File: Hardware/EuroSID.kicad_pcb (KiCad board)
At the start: 2 copper layers, 212.3 x 100 mm, 228 parts, among them J1 GATE_2, J10 IN_2, J11 IN_3, J12 PWM_CV, J13 EXT_CON, J14 Conn_01x04_Female, J15 Eurorack Connector, J16 Conn_01x06_Male, J17 Conn_ARM_JTAG_SWD_10, J18 Power_Connector_IO, J19 Power_Connector, J2 GATE_3, J20 Digital_Connector_IO, J21 CV_Connector_IO, J22 Pot_Connector_IO, J23 Attenuverter_Connector_IO, J24 Digital_Connector, J25 CV_Connector, J26 Pot_Connector, J27 Attenuverter_Connector, J28 SID_Audio_Connector_IO, J29 SID_Audio_Connector, J3 GATE_1, J4 OUT2_CON, J5 CUTOFF_CV, J6 SHAPE_CV, J7 SET_CV, J8 OUT1_CON, J9 IN_1, Q1 MMBT3904, Q2 MMBT3904, Q3 MMBT3904, SW1 Frequency Adjust, SW10 SET_SW, SW11 FILTER_SW, SW12 FILTEREXT_SW, SW13 SHAPE_SW, SW2 MOD_SW, SW3 FILTER1_SW, SW4 PROG, SW5 VOICE_SW, SW6 FILTER2_SW, SW7 RST, SW8 MODE_SW, SW9 FILTER3_SW, U1 TLC5947DAP, U10 LM1117-3.3, U11 LM1117-5.0, U12 L7809, U13 STM32F303RBTx, U2 OPA1678, U3 MCP6004, U4 MCP6004, U6 74HC595, U7 74HC595, U8 SID, U9 LM1117-3.3, X1 ECS-8FMX-010-TR

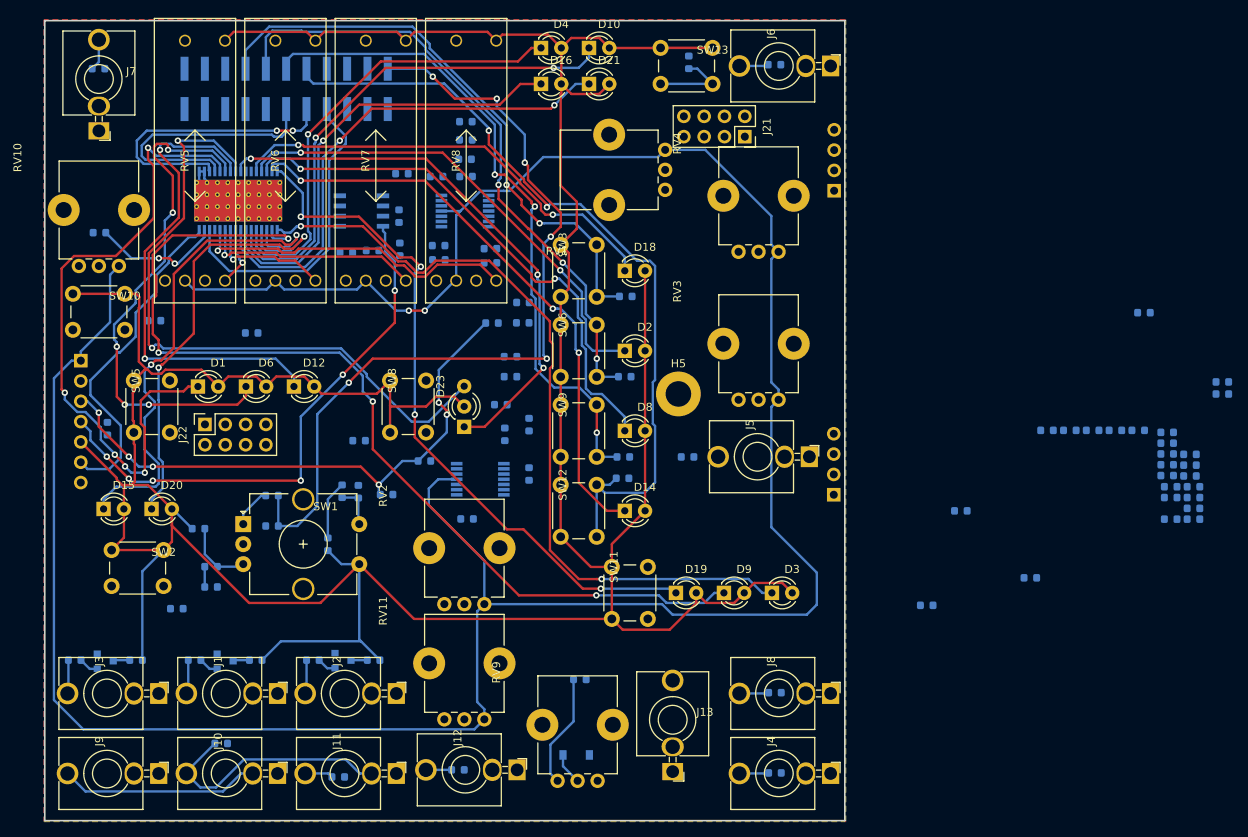
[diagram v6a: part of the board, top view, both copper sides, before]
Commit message: More wiring, removed pointless capacitors
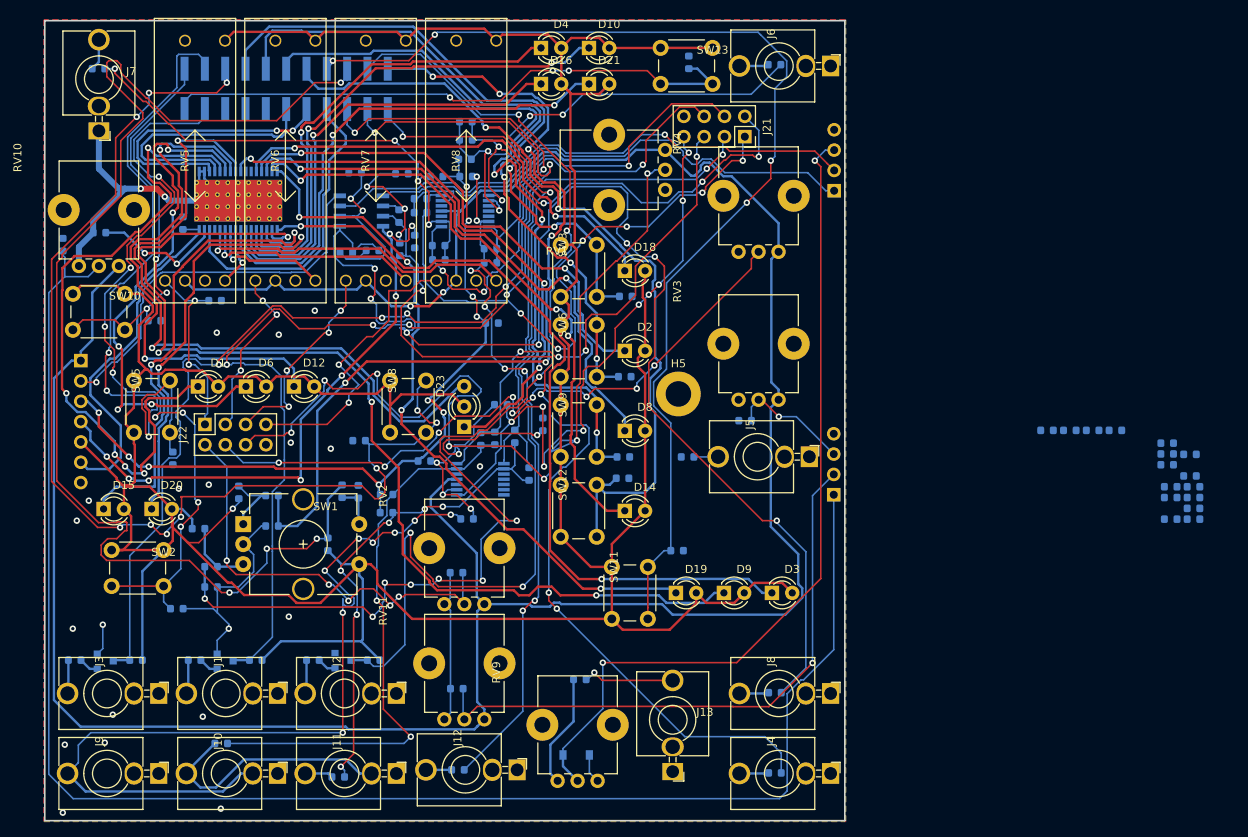
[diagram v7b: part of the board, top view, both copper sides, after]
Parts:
- moved C70 146.1 mm to (156.0, 71.0), turned to 90 degrees
- moved C15 121.0 mm to (175.1, 78.0)
- moved C3 120.7 mm to (171.0, 68.3), turned to 90 degrees
- moved C71 103.1 mm to (205.3, 126.5), turned to 180 degrees
- moved C25 97.0 mm to (200.0, 70.6), turned to 270 degrees
- moved C7 92.7 mm to (205.2, 112.0), turned to 180 degrees
- moved R4 87.1 mm to (178.0, 102.0), turned to 270 degrees
- moved R45 71.8 mm to (196.5, 104.5)
- moved C8 49.2 mm to (241.3, 93.0), turned to 180 degrees
- moved R23 44.3 mm to (232.8, 109.2)
- moved R28 23.8 mm to (192.6, 62.0)
- moved C29 18.8 mm to (200.7, 67.0)
- moved R37 18.2 mm to (200.7, 65.2)
- moved R50 10.4 mm to (210.0, 95.2), turned to 90 degrees
- moved R17 8.98 mm to (169.8, 97.7)
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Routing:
- net SET_ATTEN_IO: track 0.00 -> 204.7 mm
- net Net-(C27-Pad1): track 0.00 -> 157.1 mm, vias 0 -> 7
- net FREQ_SW_IO: track 7.37 -> 155.9 mm, vias 0 -> 4
- net FREQ_B_IO: track 2.54 -> 145.7 mm, vias 0 -> 10
- net FILTER_SW_IO: track 0.00 -> 140.2 mm, vias 0 -> 4
- net MODE_SW_IO: track 0.00 -> 140.0 mm, vias 0 -> 10
- net GATE_1_IO: track 2.12 -> 140.2 mm, vias 0 -> 6
- net GATE_2_IO: track 2.10 -> 139.3 mm, vias 0 -> 6
- net GATE_3_IO: track 2.07 -> 121.2 mm, vias 0 -> 4
- net Net-(C14-Pad1): track 0.00 -> 117.4 mm, vias 0 -> 4
- net RESONANCE_IO: track 0.00 -> 116.5 mm, vias 0 -> 7
- net SID1_EXT_IO: track 3.99 -> 104.7 mm, vias 0 -> 2
- net MOD_SW_IO: track 0.00 -> 95.6 mm, vias 0 -> 8
- net GND: track 324.5 -> 416.6 mm, vias 94 -> 110
- net Net-(C34-Pad2): track 0.00 -> 88.3 mm, vias 0 -> 8
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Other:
- net class Default: trace_width 0.25 -> 0.2
- rule trace_min: 0.2 -> 0.13
- rule via_min_size: 0.4 -> 0.6

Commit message: Finished PCB Layout
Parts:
- removed C11, C13, C19, C22: 100 nF, Capacitor_SMD:C_0603_1608Metric
- moved C17 112.0 mm to (185.1, 79.0)
- moved C26 110.7 mm to (192.5, 60.4)
- moved C24 109.7 mm to (195.5, 60.4), turned to 180 degrees
- moved C16 107.2 mm to (193.1, 79.0)
- moved C18 105.3 mm to (189.5, 93.5), turned to 90 degrees
- moved C10 102.7 mm to (192.1, 98.8), turned to 180 degrees
- moved C21 101.7 mm to (192.5, 92.7), turned to 90 degrees
- moved C20 96.2 mm to (204.1, 79.0)
- moved C12 92.8 mm to (192.0, 97.2), turned to 180 degrees
- moved C23 83.9 mm to (196.0, 82.5), turned to 180 degrees
- moved C6 75.9 mm to (230.1, 55.0)
- moved C9 64.3 mm to (237.8, 74.7), turned to 90 degrees
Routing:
- net GND: track 416.6 -> 697.1 mm, vias 110 -> 225
- net Net-(C29-Pad2): track 9.37 -> 82.4 mm, vias 0 -> 14
- net 3.3A_IO: track 340.0 -> 363.0 mm, vias 2 -> 6
- net CUTOFF_IO: track 84.3 -> 92.9 mm
- net -12V_IO: track 50.8 -> 57.8 mm
- net FILTEREXT_SW_IO: track 103.5 -> 108.6 mm
- net SID1_EXT_IO: track 104.7 -> 109.7 mm
- net FILTER2_SW_IO: track 87.5 -> 92.5 mm
- net RELEASE_IO: track 36.5 -> 41.5 mm, vias 2 -> 3
- net RESONANCE_IO: track 116.5 -> 121.2 mm, vias 7 -> 8
- net 12V_IO: track 75.5 -> 79.6 mm, vias 8 -> 9
- net +3.3VA: track 120.5 -> 124.0 mm
- net Net-(C27-Pad1): track 157.1 -> 160.2 mm, vias 7 -> 9
- net MODE_SW_IO: track 140.0 -> 142.9 mm
- net Net-(C34-Pad2): track 88.3 -> 90.9 mm
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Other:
- rule trace_min: 0.13 -> 0.2
